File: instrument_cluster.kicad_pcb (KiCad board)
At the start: 2 copper layers, 144.8 x 45.7 mm, 76 parts, among them J1 Conn_02x16_Top_Bottom, J2 Conn_02x16_Top_Bottom, J3 USB mini-B SMD, J4 NOT_FITTED_SWD_Conn_01x04_Male, J5 54819-0572, J6 NOT_FITTED_SWD_Conn_01x04_Male, U1 LM2575S-5.0_NOPB, U10 74HC4050D, U11 TJA1040T, U12 TJA1040T, U2 LM2575S-5.0_NOPB, U3 LD1117S33TR_SOT223, U4 LD1117S33TR_SOT223, U5 STM32F105RBTx, U6 TJA1040T, U7 TJA1040T, U8 74HC4050D, U9 STM32F105RBTx, Y1 Crystal KX-13 25MHz, Y2 Crystal KX-13 25MHz

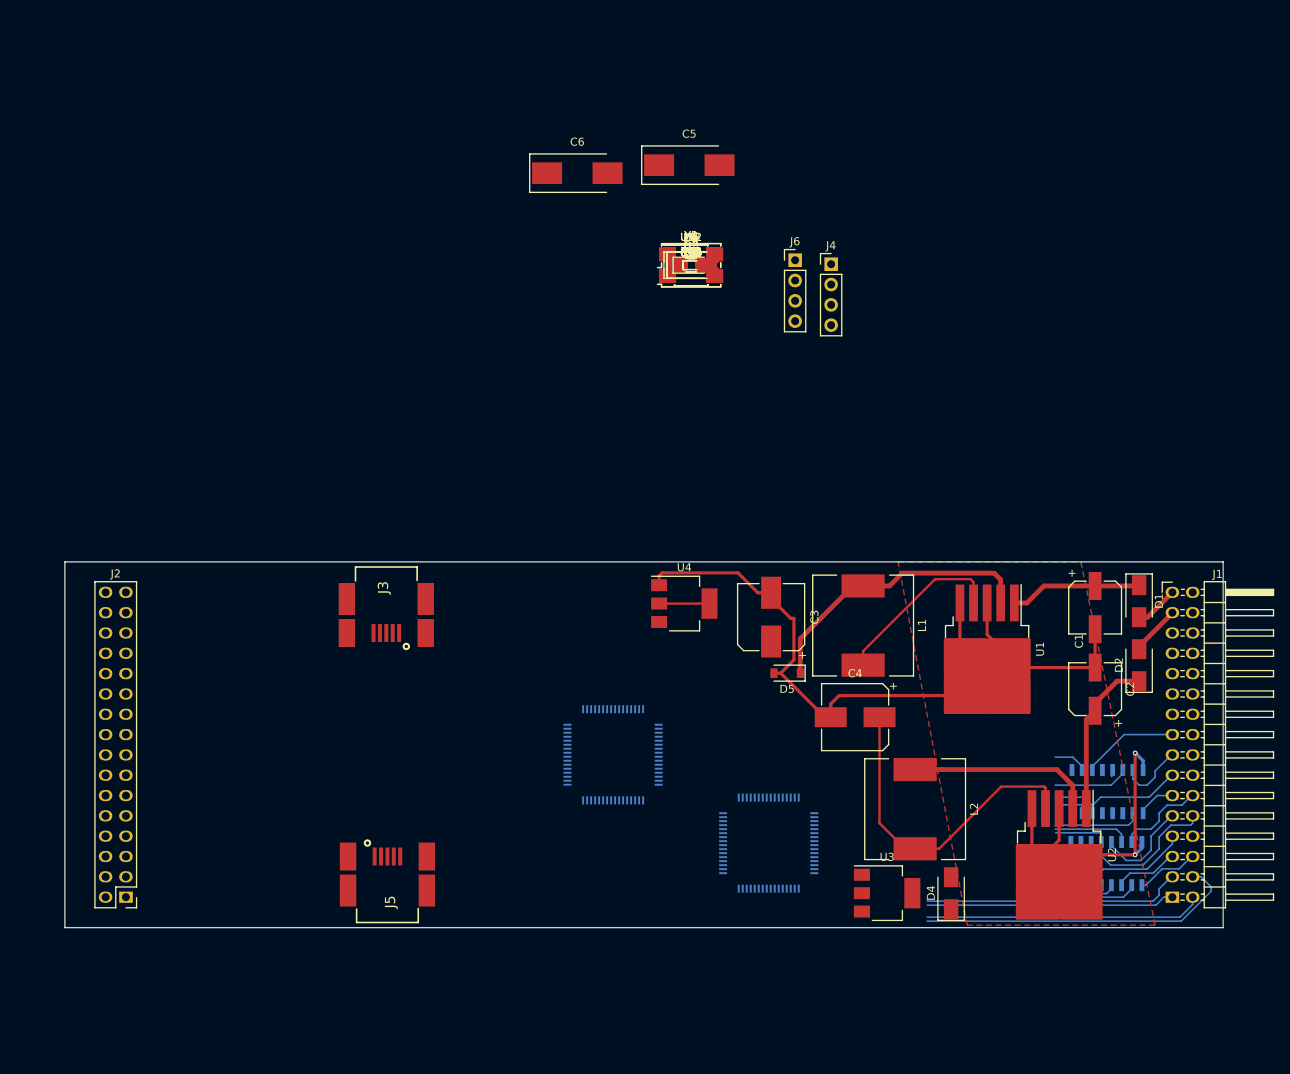
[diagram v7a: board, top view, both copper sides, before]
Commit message: fill both side with GND, add heat exchange with lm2575
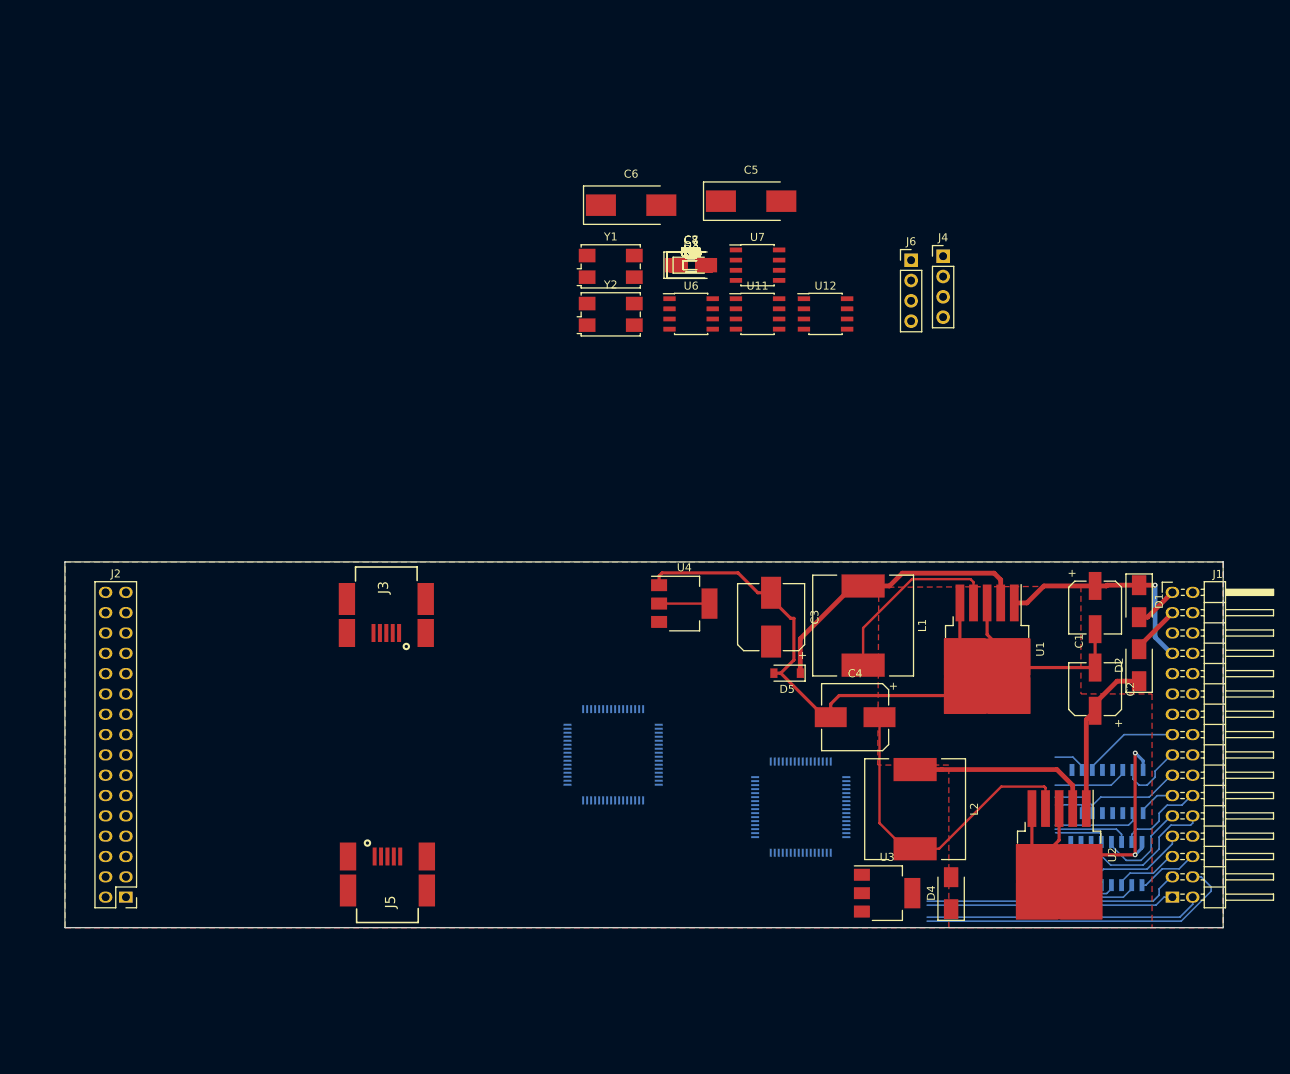
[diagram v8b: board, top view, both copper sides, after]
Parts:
- moved U12 17.9 mm to (157.3, 54.1)
- moved J6 14.5 mm to (168.0, 47.4)
- moved J4 14.0 mm to (172.0, 46.9)
- moved Y2 11.8 mm to (130.4, 54.1)
- moved U11 10.3 mm to (148.8, 54.1)
- moved Y1 10.1 mm to (130.4, 48.1)
- moved C5 8.94 mm to (148.0, 40.0)
- moved U7 8.30 mm to (148.8, 48.0)
- moved C6 7.82 mm to (133.0, 40.5)
- moved U6 6.09 mm to (140.5, 54.1)
- moved U9 6.02 mm to (154.2, 115.8)
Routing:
- net /FUEL_TANK_in: track 16.9 -> 28.0 mm, vias 0 -> 1
- net /power_supply/+5V_B_module: track 22.0 -> 23.7 mm
- added copper zone on B.Cu, net GND
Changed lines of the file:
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@@
   (general
     (links 242)
-    (no_connects 136)
+    (no_connects 147)
     (area 62.154999 85.014999 207.085001 130.885001)
     (thickness 1.6)
     (drawings 12)
-    (tracks 200)
+    (tracks 203)
     (zones 0)
     (modules 76)
@@
   )
   (module Capacitors_Tantalum_SMD:CP_Tantalum_Case-D_EIA-7343-31_Hand (layer F.Cu)
-    (at 140.275 35.5)
+    (at 148 40)
     (descr "Tantalum capacitor, Case D, EIA 7343-31, 7.3x4.3x2.8mm, Hand soldering footprint")
     (tags "capacitor tantalum smd")
@@
   )
   (module Capacitors_Tantalum_SMD:CP_Tantalum_Case-D_EIA-7343-31_Hand (layer F.Cu)
-    (at 126.275 36.5)
+    (at 133 40.5)
     (descr "Tantalum capacitor, Case D, EIA 7343-31, 7.3x4.3x2.8mm, Hand soldering footprint")
     (tags "capacitor tantalum smd")
@@
   )
   (module Pin_Headers:Pin_Header_Straight_1x04_Pitch2.54mm (layer F.Cu)
-    (at 158 47.88)
+    (at 172 46.88)
     (descr "Through hole straight pin header, 1x04, 2.54mm pitch, single row")
     (tags "Through hole pin header THT 1x04 2.54mm single row")
@@
   )
   (module Pin_Headers:Pin_Header_Straight_1x04_Pitch2.54mm (layer F.Cu)
-    (at 153.5 47.38)
+    (at 168 47.38)
     (descr "Through hole straight pin header, 1x04, 2.54mm pitch, single row")
     (tags "Through hole pin header THT 1x04 2.54mm single row")
@@
   )
   (module Housings_SOIC:SOIC-8_3.9x4.9mm_Pitch1.27mm (layer F.Cu)
-    (at 140.5011 48.0036)
+    (at 140.5011 54.095)
     (descr "8-Lead Plastic Small Outline (SN) - Narrow, 3.90 mm Body [SOIC] (see Microchip Packaging Specification 00000049BS.pdf)")
     (tags "SOIC 1.27")
@@
   )
   (module Housings_SOIC:SOIC-8_3.9x4.9mm_Pitch1.27mm (layer F.Cu)
-    (at 140.5011 48.0036)
+    (at 148.8 48.0036)
     (descr "8-Lead Plastic Small Outline (SN) - Narrow, 3.90 mm Body [SOIC] (see Microchip Packaging Specification 00000049BS.pdf)")
     (tags "SOIC 1.27")
@@
   )
   (module Housings_SOIC:SOIC-8_3.9x4.9mm_Pitch1.27mm (layer F.Cu)
-    (at 140.5011 48.0036)
+    (at 148.8 54.095)
     (descr "8-Lead Plastic Small Outline (SN) - Narrow, 3.90 mm Body [SOIC] (see Microchip Packaging Specification 00000049BS.pdf)")
     (tags "SOIC 1.27")
@@
   )
   (module Housings_SOIC:SOIC-8_3.9x4.9mm_Pitch1.27mm (layer F.Cu)
-    (at 140.5011 48.0036)
+    (at 157.3 54.095)
     (descr "8-Lead Plastic Small Outline (SN) - Narrow, 3.90 mm Body [SOIC] (see Microchip Packaging Specification 00000049BS.pdf)")
     (tags "SOIC 1.27")
@@
   )
   (module Crystals:Crystal_SMD_7050-4pin_7.0x5.0mm (layer F.Cu)
-    (at 140.5011 48.0036)
+    (at 130.45 48.15)
     (descr "SMD Crystal SERIES SMD7050/4 https://www.foxonline.com/pdfs/FQ7050.pdf, 7.0x5.0mm^2 package")
     (tags "SMD SMT crystal")
@@
   )
   (module Crystals:Crystal_SMD_7050-4pin_7.0x5.0mm (layer F.Cu)
-    (at 140.5011 48.0036)
+    (at 130.45 54.15)
     (descr "SMD Crystal SERIES SMD7050/4 https://www.foxonline.com/pdfs/FQ7050.pdf, 7.0x5.0mm^2 package")
     (tags "SMD SMT crystal")
@@
   )
   (module Housings_QFP:LQFP-64_10x10mm_Pitch0.5mm (layer B.Cu)
-    (at 150.2 120.25)
+    (at 154.2 115.75)
     (descr "64 LEAD LQFP 10x10mm (see MICREL LQFP10x10-64LD-PL-1.pdf)")
     (tags "QFP 0.5")
@@
     (arrow2b (pts (xy 223.259218 130.81) (xy 222.672797 129.683496)))
   )
+  (segment (start 198.5 88) (end 198.5 94.51) (width 0.6) (layer B.Cu) (net 1))
+  (segment (start 198.5 94.51) (end 200.51 96.52) (width 0.6) (layer B.Cu) (net 1))
+  (segment (start 200.51 96.52) (end 200.66 96.52) (width 0.6) (layer B.Cu) (net 1))
+  (segment (start 196.5 88) (end 198.5 88) (width 0.6) (layer F.Cu) (net 1))
+  (via (at 198.5 88) (size 0.6) (drill 0.3) (layers F.Cu B.Cu) (net 1))
+  (segment (start 192.4 88.1) (end 192.5 88) (width 0.6) (layer F.Cu) (net 1))
+  (segment (start 192.5 88) (end 196.5 88) (width 0.6) (layer F.Cu) (net 1))
+  (segment (start 191 88.1) (end 192.4 88.1) (width 0.6) (layer F.Cu) (net 1))
   (segment (start 184.6 88.1) (end 182.475 90.225) (width 0.6) (layer F.Cu) (net 1))
   (segment (start 182.475 90.225) (end 180.9 90.225) (width 0.6) (layer F.Cu) (net 1))
   (segment (start 191 88.1) (end 184.6 88.1) (width 0.6) (layer F.Cu) (net 1))
-  (segment (start 196.5 88) (end 196.5 88.35) (width 0.6) (layer F.Cu) (net 1))
-  (segment (start 191 88.1) (end 196.4 88.1) (width 0.6) (layer F.Cu) (net 1))
-  (segment (start 196.4 88.1) (end 196.5 88) (width 0.6) (layer F.Cu) (net 1))
   (segment (start 196.02521 108.97521) (end 196.01356 108.97521) (width 0.4) (layer B.Cu) (net 2))
   (segment (start 197 109.95) (end 196.02521 108.97521) (width 0.4) (layer B.Cu) (net 2))
@@
   (segment (start 194.62 106.68) (end 190.65 110.65) (width 0.2) (layer B.Cu) (net 28))
   (segment (start 190.65 110.65) (end 190.65 111.1) (width 0.2) (layer B.Cu) (net 28))
-  (segment (start 190.54 111.05) (end 190.54 111.5) (width 0.2) (layer B.Cu) (net 28))
   (segment (start 201.6 129.5) (end 170 129.5) (width 0.2) (layer B.Cu) (net 30))
   (segment (start 203.2 127) (end 203.2 127.9) (width 0.2) (layer B.Cu) (net 30))
@@
   (segment (start 195.58 125.5) (end 195.58 125.95) (width 0.2) (layer B.Cu) (net 61))
   (segment (start 195.58 125.95) (end 194.53 127) (width 0.2) (layer B.Cu) (net 61))
-  (segment (start 175.42501 87.25001) (end 170.99999 87.25001) (width 0.3) (layer F.Cu) (net 66))
-  (segment (start 170.99999 87.25001) (end 162 96.25) (width 0.3) (layer F.Cu) (net 66))
-  (segment (start 162 96.25) (end 162 98) (width 0.3) (layer F.Cu) (net 66))
   (segment (start 175.8 90.225) (end 175.8 87.625) (width 0.3) (layer F.Cu) (net 66))
   (segment (start 175.8 87.625) (end 175.42501 87.25001) (width 0.3) (layer F.Cu) (net 66))
+  (segment (start 175.42501 87.25001) (end 168.10378 87.25001) (width 0.3) (layer F.Cu) (net 66))
+  (segment (start 168.10378 87.25001) (end 162 93.35379) (width 0.3) (layer F.Cu) (net 66))
+  (segment (start 162 93.35379) (end 162 98) (width 0.3) (layer F.Cu) (net 66))
   (segment (start 164.05 104.5) (end 164.05 117.75) (width 0.3) (layer F.Cu) (net 67))
   (segment (start 164.05 117.75) (end 167.25 120.95) (width 0.3) (layer F.Cu) (net 67))
@@
   (segment (start 189.38 115.55) (end 189.279999 115.449999) (width 0.2) (layer B.Cu) (net 186))
   (segment (start 189.279999 115.449999) (end 186.050001 115.449999) (width 0.2) (layer B.Cu) (net 186))
-  (segment (start 193.08 111.95) (end 193.08 111.5) (width 0.2) (layer B.Cu) (net 188))
   (zone (net 2) (net_name GND) (layer F.Cu) (hatch none 0.508)
     (priority 1)
-    (connect_pads thru_hole_only (clearance 0.3))
+    (connect_pads thru_hole_only (clearance 0.5))
+    (min_thickness 0.0254)
+    (fill yes (mode segment) (arc_segments 32) (thermal_gap 0.508) (thermal_bridge_width 0.508))
+    (polygon
+      (pts
+        (xy 163.957 88.265) (xy 189.23 88.138) (xy 189.23 101.6) (xy 198.12 101.6) (xy 198.12 130.81)
+        (xy 172.72 130.81) (xy 172.72 110.49) (xy 163.83 110.49)
+      )
+    )
+  )
+  (zone (net 2) (net_name GND) (layer F.Cu) (hatch full 0.508)
+    (connect_pads (clearance 0.3))
+    (min_thickness 0.0254)
+    (fill yes (mode segment) (arc_segments 32) (thermal_gap 0.508) (thermal_bridge_width 0.508) (smoothing chamfer) (radius 2))
+    (polygon
+      (pts
+        (xy 207.01 85.09) (xy 207.01 130.81) (xy 62.23 130.81) (xy 62.23 85.09)
+      )
+    )
+  )
+  (zone (net 2) (net_name GND) (layer B.Cu) (hatch full 0.508)
+    (connect_pads (clearance 0.3))
     (min_thickness 0.0254)
-    (fill (mode segment) (arc_segments 32) (thermal_gap 0.508) (thermal_bridge_width 0.508) (smoothing chamfer) (radius 2))
+    (fill yes (mode segment) (arc_segments 32) (thermal_gap 0.508) (thermal_bridge_width 0.508) (smoothing chamfer) (radius 2))
     (polygon
       (pts
-        (xy 166.37 85.09) (xy 189.23 85.09) (xy 198.5 130.5) (xy 175 130.5)
+        (xy 207.01 85.09) (xy 207.01 130.81) (xy 62.23 130.81) (xy 62.23 85.09)
       )
     )
